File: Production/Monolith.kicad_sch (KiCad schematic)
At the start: 0 parts

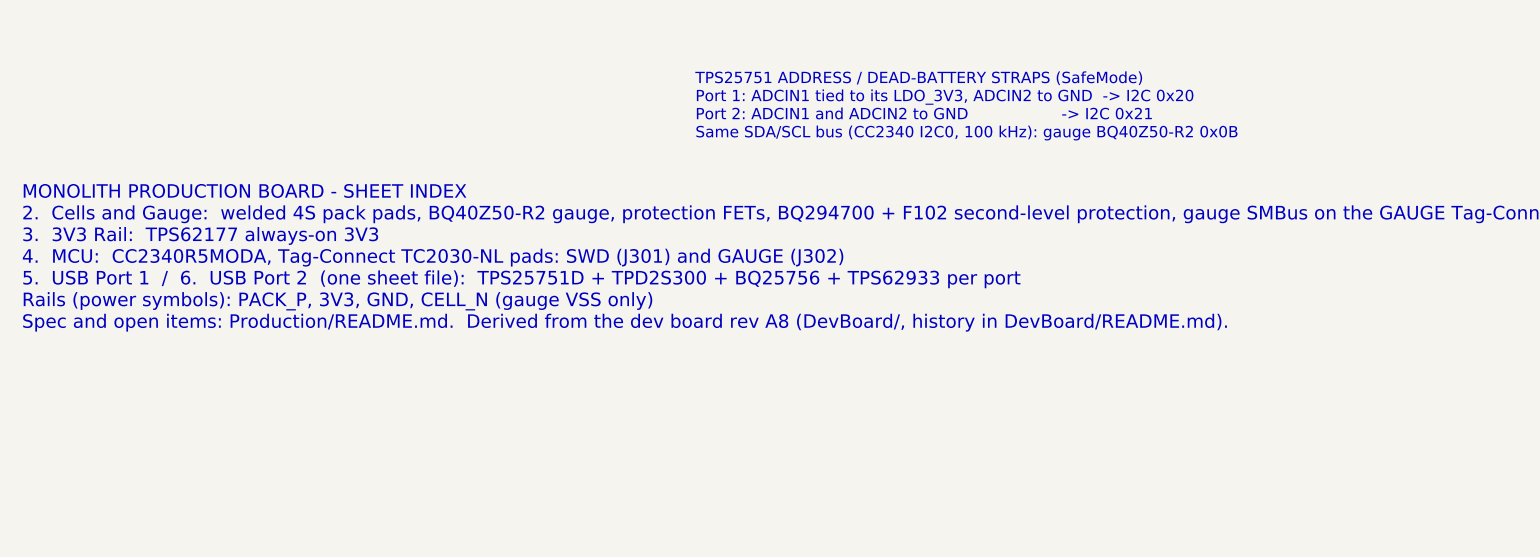
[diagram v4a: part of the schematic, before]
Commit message: Production: U405/U505 TPD2S300 -> TPD6S300 (no via-in-pad)
The TPD2S300's WCSP-9 centre ball needed a 0.15 mm via-in-pad, below
JLC's no-surcharge hole size and the project's 0.3 mm drill rule. The
TPD6S300RUKR (WQFN-20 3x3, LCSC C2649810) does the same CC job
(24 V short-to-VBUS OVP, IEC ESD, FLT) and fans out with standard vias.

- tools/tpd6s300.py: symbol, pin nets, and a footprint from KiCad's
  RUK0020B with four 0.3/0.5 mm vias in the exposed pad
- RPD_G1/G2 -> C_CC1/C_CC2 for dead-battery Rd; SBU and D1/D2 unused
- board: footprints swapped in place, U405 moved 0.65 mm clear of U401
- IVPWR is 90 uA typ per part (TPD2S300: 3.2 uA), noted in the README

Co-Authored-By: Claude Opus 5.5 <noreply@anthropic.com>
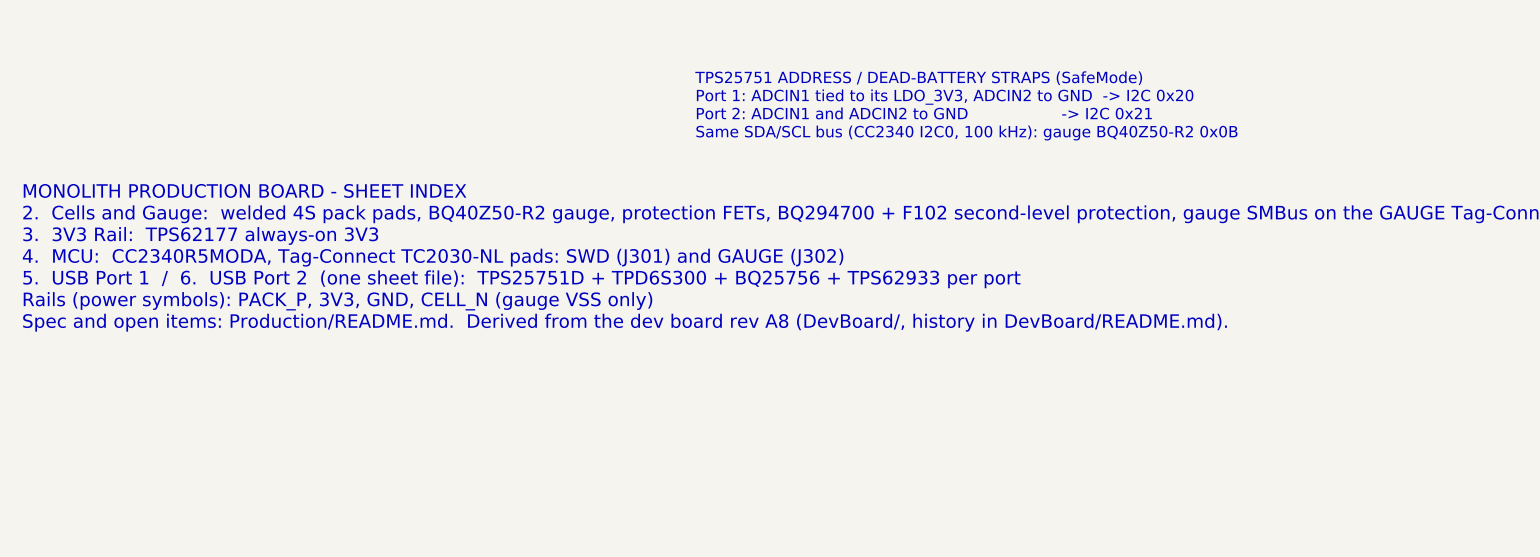
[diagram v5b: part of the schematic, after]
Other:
- note added: "MONOLITH PRODUCTION BOARD - SHEET INDEX 2. Cells and Gauge: welded 4S pack pads, BQ40Z50-R2 gauge, protection FETs, BQ294700 + F102 second-level protection, gauge SMBus on the GAUGE Tag-Connect (MCU sheet) 3. 3V3 Rail: TPS62177 always-on 3V3 4. MCU: CC2340R5MODA, Tag-Connect TC2030-NL pads: SWD (J301) and GAUGE (J302) 5. USB Port 1 / 6. USB Port 2 (one sheet file): TPS25751D + TPD6S300 + BQ25756 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"
- note removed: "MONOLITH PRODUCTION BOARD - SHEET INDEX 2. Cells and Gauge: welded 4S pack pads, BQ40Z50-R2 gauge, protection FETs, BQ294700 + F102 second-level protection, gauge SMBus on the GAUGE Tag-Connect (MCU sheet) 3. 3V3 Rail: TPS62177 always-on 3V3 4. MCU: CC2340R5MODA, Tag-Connect TC2030-NL pads: SWD (J301) and GAUGE (J302) 5. USB Port 1 / 6. USB Port 2 (one sheet file): TPS25751D + TPD2S300 + BQ25756 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"
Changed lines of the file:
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@@
 		(comment 3 "P0: dev board rev A8 stripped by Production/tools/make_production.py; not reviewed")
 	)
-	(text "MONOLITH PRODUCTION BOARD - SHEET INDEX\n2.  Cells and Gauge:  welded 4S pack pads, BQ40Z50-R2 gauge, protection FETs, BQ294700 + F102 second-level protection, gauge SMBus on the GAUGE Tag-Connect (MCU sheet)\n3.  3V3 Rail:  TPS62177 always-on 3V3\n4.  MCU:  CC2340R5MODA, Tag-Connect TC2030-NL pads: SWD (J301) and GAUGE (J302)\n5.  USB Port 1  /  6.  USB Port 2  (one sheet file):  TPS25751D + TPD2S300 + BQ25756 + TPS62933 per port\nRails (power symbols): PACK_P, 3V3, GND, CELL_N (gauge VSS only)\nSpec and open items: Production/README.md.  Derived from the dev board rev A8 (DevBoard/, history in DevBoard/README.md)."
+	(text "MONOLITH PRODUCTION BOARD - SHEET INDEX\n2.  Cells and Gauge:  welded 4S pack pads, BQ40Z50-R2 gauge, protection FETs, BQ294700 + F102 second-level protection, gauge SMBus on the GAUGE Tag-Connect (MCU sheet)\n3.  3V3 Rail:  TPS62177 always-on 3V3\n4.  MCU:  CC2340R5MODA, Tag-Connect TC2030-NL pads: SWD (J301) and GAUGE (J302)\n5.  USB Port 1  /  6.  USB Port 2  (one sheet file):  TPS25751D + TPD6S300 + BQ25756 + TPS62933 per port\nRails (power symbols): PACK_P, 3V3, GND, CELL_N (gauge VSS only)\nSpec and open items: Production/README.md.  Derived from the dev board rev A8 (DevBoard/, history in DevBoard/README.md)."
 		(exclude_from_sim no)
 		(at 30.48 205.74 0)
